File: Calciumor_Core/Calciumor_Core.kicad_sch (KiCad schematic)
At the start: 139 parts, among them J1 Conn_01x07_Pin, J2 USB_C_Main, J4 NeoPixel, J5 Li-Po(PH_S2B_SMD), J6 Conn_01x05_Pin, Q1 2SC4116, Q2 2SC4116, SW1 SW_Push, SW10 SW_Push, SW11 SW_Push, SW12 SW_Push, SW13 SW_Push, SW14 SW_Push, SW15 SW_Push, SW16 SW_Push, SW17 SW_Push, SW18 SW_Push, SW19 TMHU27, SW2 SW_Push, SW20 Power_SW, SW21 Program, SW22 Reset, SW3 SW_Push, SW4 RotaryEncoder_Switch, SW5 SW_Push, SW6 SW_Push, SW7 SW_Push, SW8 SW_Push, SW9 SW_Push, U1 LM324APT, U10 AE-XC9306-5V, U2 NJM12877F25, U3 ESP32-S3-WROOM-1-N16R8, U4 MCP73831-2-OT, U5 BD5229G-1, U6 FT231XS, U7 NC7SV157, U8 XC6194AA05ER-G, U9 AE-XC9306-3V3

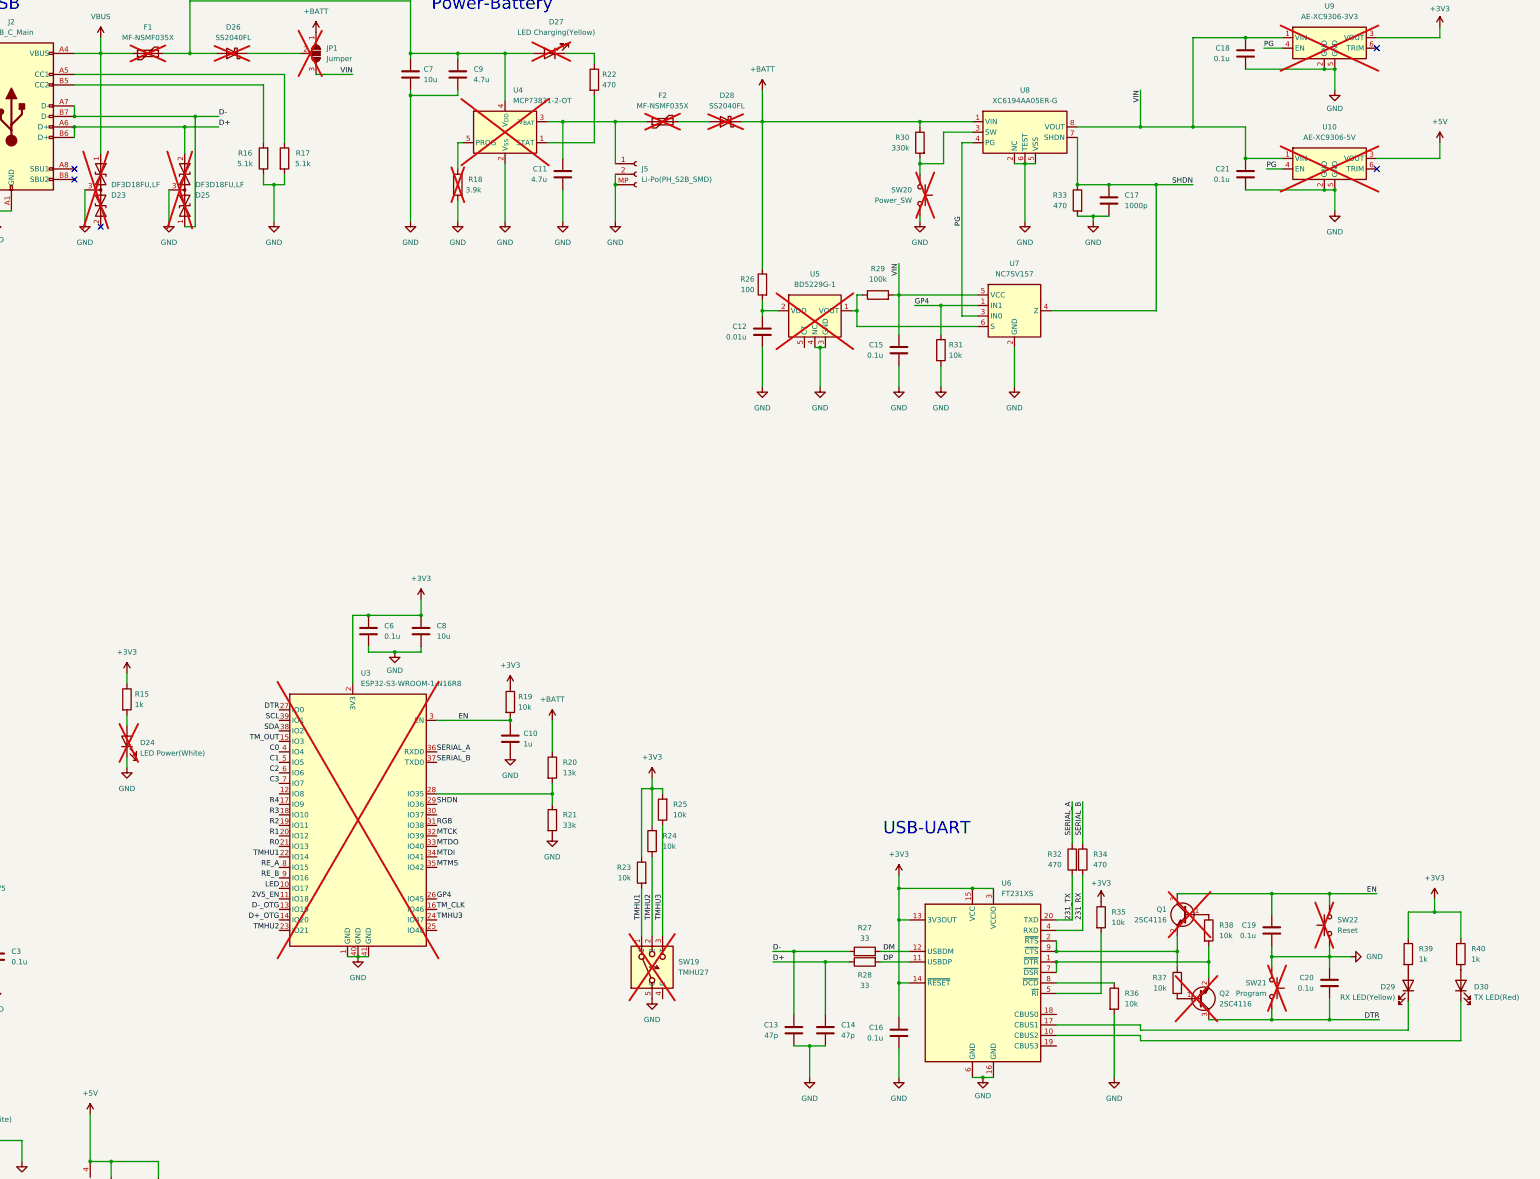
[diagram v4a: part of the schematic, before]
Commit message: Changed to native USB
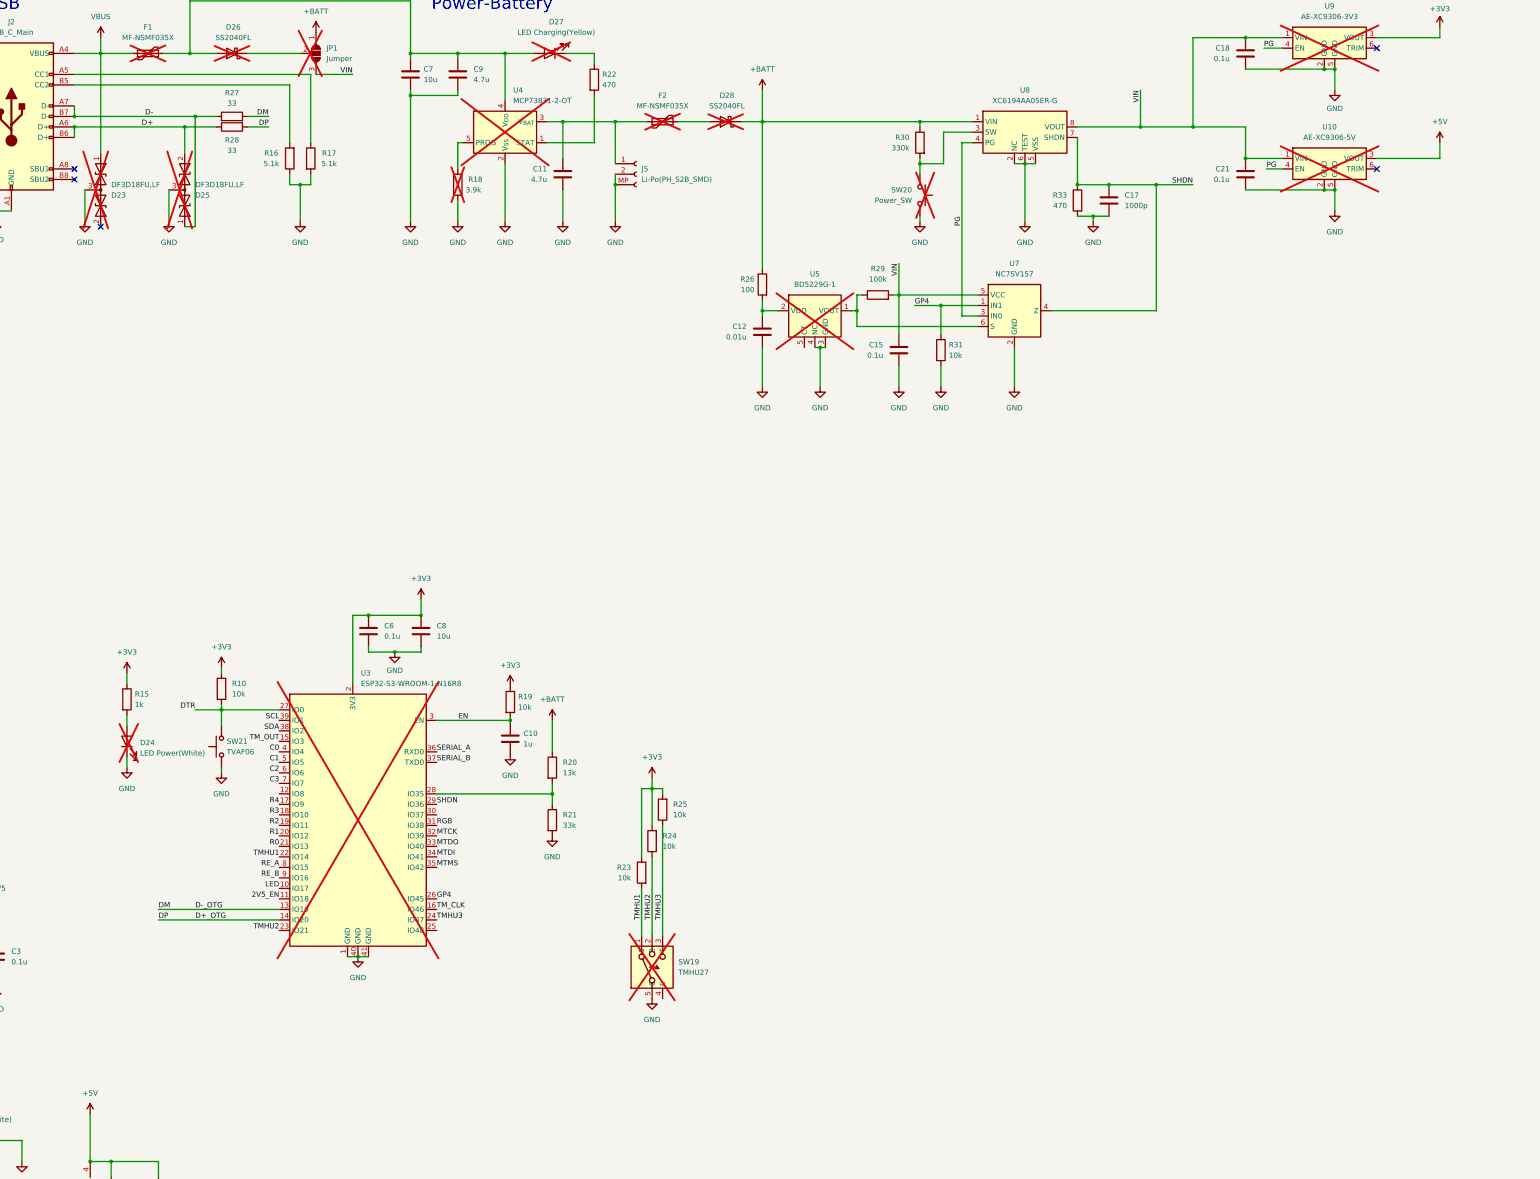
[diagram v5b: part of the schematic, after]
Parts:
- removed C13, C14: 47p, Capacitor_SMD:C_0402_1005Metric, symbol Device:C
- removed C16, C19, C20: 0.1u, Capacitor_SMD:C_0402_1005Metric, symbol Device:C
- removed D29: RX LED(Yellow), LED_SMD:LED_0603_1608Metric, symbol Device:LED
- removed D30: TX LED(Red), LED_SMD:LED_0603_1608Metric, symbol Device:LED
- removed Q1, Q2: 2SC4116, Package_TO_SOT_SMD:SOT-323_SC-70, symbol Transistor_BJT:2SC4213
- removed R32, R34: 470, Resistor_SMD:R_0402_1005Metric, symbol Device:R
- removed R35, R36, R37, R38: 10k, Resistor_SMD:R_0402_1005Metric, symbol Device:R
- removed R39, R40: 1k, Resistor_SMD:R_0402_1005Metric, symbol Device:R
- removed SW22: Reset, Ultramarine-2:TVAF06, symbol Switch:SW_Push
- removed U6: FT231XS, Package_SO:SSOP-20_3.9x8.7mm_P0.635mm, symbol Interface_USB:FT231XS
- added R10: 10k, Resistor_SMD:R_0402_1005Metric, symbol Device:R
- SW21: value Program -> TVAF06; now fitted
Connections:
- net DM is gone; now on net D-_OTG: R27.2
- net DP is gone; now on net D+_OTG: R28.2
- net +3V3: now also R10.2
- net DTR: now also SW21.2, R10.1; no longer SW21.1
- net GND: now also SW21.1; no longer SW21.2
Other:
- note removed: "USB-UART"
- moved on the sheet: R16, R17, R27, R28

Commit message: Core_rev1.0
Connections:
- net GND: now also SW20.2, SW20.MP; no longer SW20.1
- net at R30.2, U8.3 (SW): now also SW20.1; no longer SW20.2
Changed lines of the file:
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@@
 	)
 	(junction
+		(at 378.46 68.58)
+		(diameter 0)
+		(color 0 0 0 0)
+	)
+	(junction
 		(at 373.38 87.63)
 		(diameter 0)
@@
 	(wire
 		(pts
+			(xy 375.92 58.42) (xy 365.76 58.42)
+		)
+		(stroke
+			(width 0)
+			(type default)
+		)
+	)
+	(wire
+		(pts
 			(xy 466.09 27.94) (xy 461.645 27.94)
 		)
@@
 	(wire
 		(pts
+			(xy 365.76 68.58) (xy 378.46 68.58)
+		)
+		(stroke
+			(width 0)
+			(type default)
+		)
+	)
+	(wire
+		(pts
 			(xy 383.54 90.17) (xy 383.54 97.155)
 		)
@@
 	(wire
 		(pts
+			(xy 365.76 58.42) (xy 365.76 68.58)
+		)
+		(stroke
+			(width 0)
+			(type default)
+		)
+	)
+	(wire
+		(pts
 			(xy 66.04 156.21) (xy 104.14 156.21)
 		)
@@
 	)
 	(symbol
+		(lib_name "SW_Push_1")
 		(lib_id "Switch:SW_Push")
 		(at 378.46 63.5 270)
-		(mirror x)
 		(unit 1)
 		(exclude_from_sim no)
@@
 		(dnp yes)
 		(property "Reference" "SW20"
-			(at 376.555 62.23 90)
+			(at 376.555 64.77 90)
 			(effects
 				(font
@@
 		)
 		(property "Value" "Power_SW"
-			(at 376.555 64.77 90)
+			(at 376.555 62.23 90)
 			(effects
 				(font
@@
 		(pin "2"
 		)
+		(pin "MP"
+		)
 		(instances
